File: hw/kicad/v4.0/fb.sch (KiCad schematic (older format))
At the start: 48 parts, among them J1 RJ45_LED, U15 SN65176B, U16 SN65176B, U19 SN65176B, U7 LM358

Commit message: Changed 120uf 1808 to 1210 100uF
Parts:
- C116, C117, C118, C12, C125, C37, C71, C73, C76: LCSC C14663 -> C14663
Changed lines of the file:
@@
 F 9 "" H 0   0   50  0001 C CNN "Description"
 F 10 "" H 0   0   50  0001 C CNN "Manufacturer"
-F 11 " C14663" H 9200 1250 50  0001 C CNN "LCSC"
+F 11 "C14663" H 9200 1250 50  0001 C CNN "LCSC"
 	1    9200 1250
 	1    0    0    -1
@@
 F 9 "" H 0   0   50  0001 C CNN "Description"
 F 10 "" H 0   0   50  0001 C CNN "Manufacturer"
-F 11 " C14663" H 9200 2650 50  0001 C CNN "LCSC"
+F 11 "C14663" H 9200 2650 50  0001 C CNN "LCSC"
 	1    9200 2650
 	1    0    0    -1
@@
 F 9 "" H 0   0   50  0001 C CNN "Description"
 F 10 "" H 0   0   50  0001 C CNN "Manufacturer"
-F 11 " C14663" H 9200 4050 50  0001 C CNN "LCSC"
+F 11 "C14663" H 9200 4050 50  0001 C CNN "LCSC"
 	1    9200 4050
 	1    0    0    -1
@@
 F 9 "" H 0   0   50  0001 C CNN "Description"
 F 10 "" H 0   0   50  0001 C CNN "Manufacturer"
-F 11 " C14663" H 2700 6800 50  0001 C CNN "LCSC"
+F 11 "C14663" H 2700 6800 50  0001 C CNN "LCSC"
 	1    2700 6800
 	1    0    0    -1
@@
 F 9 "" H 0   0   50  0001 C CNN "Description"
 F 10 "" H 0   0   50  0001 C CNN "Manufacturer"
-F 11 " C14663" H 3100 5750 50  0001 C CNN "LCSC"
+F 11 "C14663" H 3100 5750 50  0001 C CNN "LCSC"
 	1    3100 5750
 	-1   0    0    1
@@
 F 9 "" H 0   0   50  0001 C CNN "Description"
 F 10 "" H 0   0   50  0001 C CNN "Manufacturer"
-F 11 " C14663" H 1700 5500 50  0001 C CNN "LCSC"
+F 11 "C14663" H 1700 5500 50  0001 C CNN "LCSC"
 	1    1700 5500
 	-1   0    0    1
@@
 F 9 "" H 0   0   50  0001 C CNN "Description"
 F 10 "" H 0   0   50  0001 C CNN "Manufacturer"
-F 11 " C14663" H 10700 1050 50  0001 C CNN "LCSC"
+F 11 "C14663" H 10700 1050 50  0001 C CNN "LCSC"
 	1    10700 1050
 	1    0    0    1
@@
 F 9 "" H 0   0   50  0001 C CNN "Description"
 F 10 "" H 0   0   50  0001 C CNN "Manufacturer"
-F 11 " C14663" H 2500 3900 50  0001 C CNN "LCSC"
+F 11 "C14663" H 2500 3900 50  0001 C CNN "LCSC"
 	1    2500 3900
 	1    0    0    -1
@@
 F 9 "" H 0   0   50  0001 C CNN "Description"
 F 10 "" H 0   0   50  0001 C CNN "Manufacturer"
-F 11 " C14663" H 2450 4750 50  0001 C CNN "LCSC"
+F 11 "C14663" H 2450 4750 50  0001 C CNN "LCSC"
 	1    2450 4750
 	1    0    0    -1

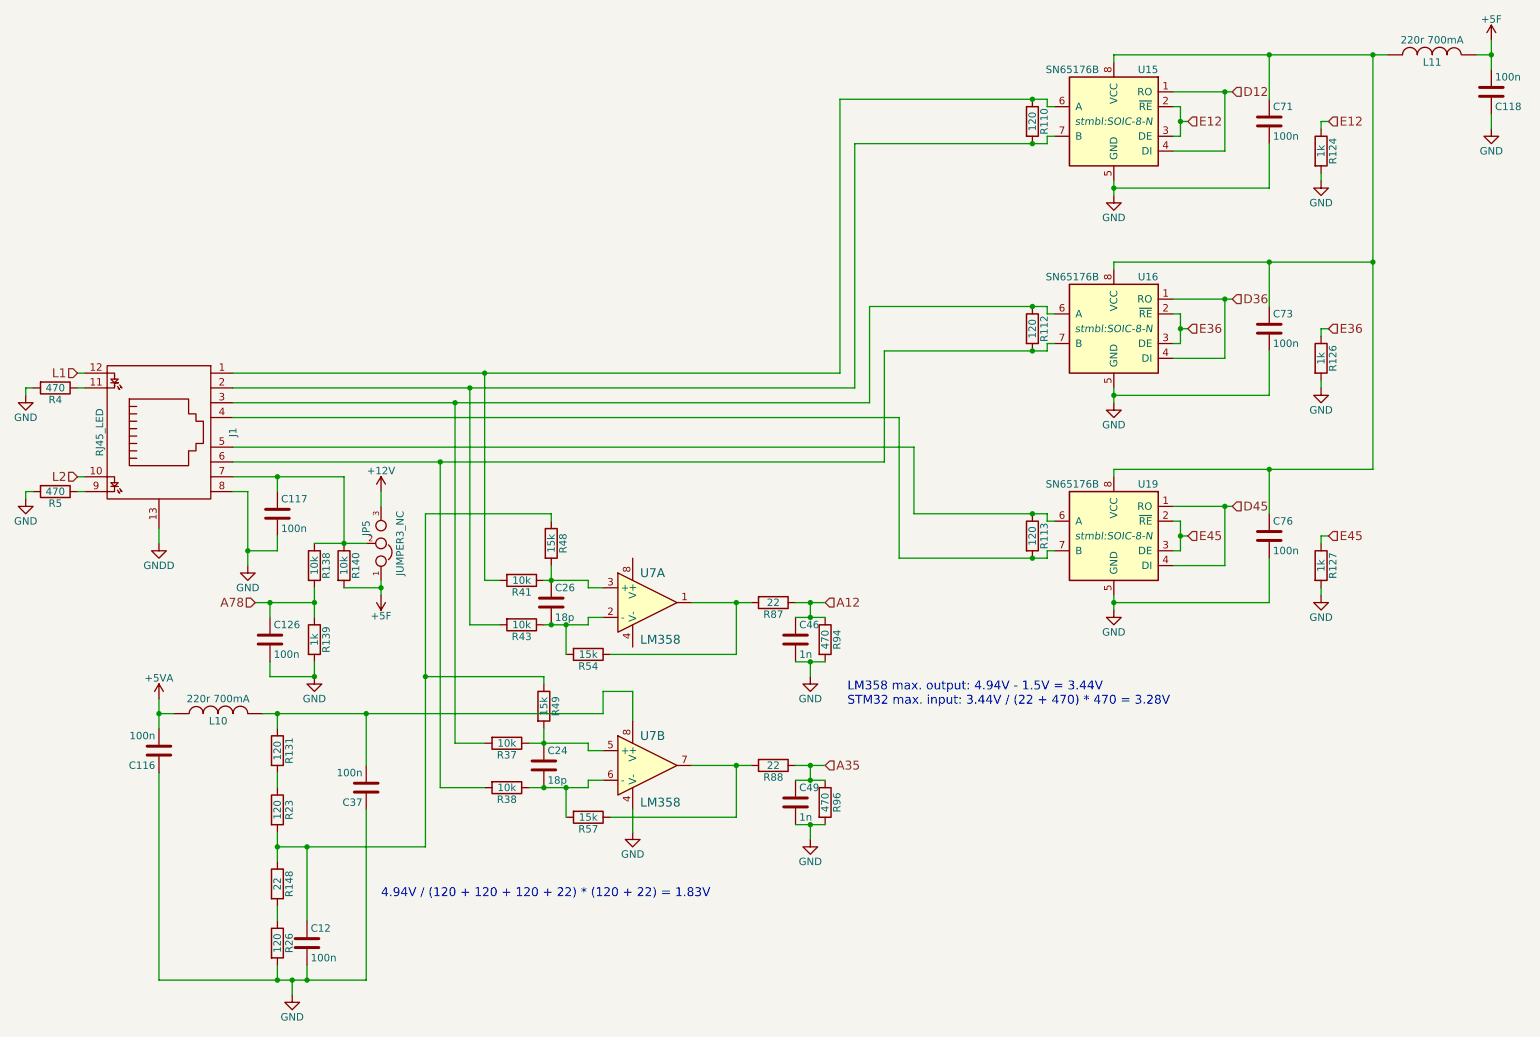
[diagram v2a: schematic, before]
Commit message: Switch some 2.2uf 0603 to 1uf bypass to get 50V version on jlcpcb
Change 2.2uf 0603 to 0805 on iram to get 50V version on jlcpcb
other cleanup
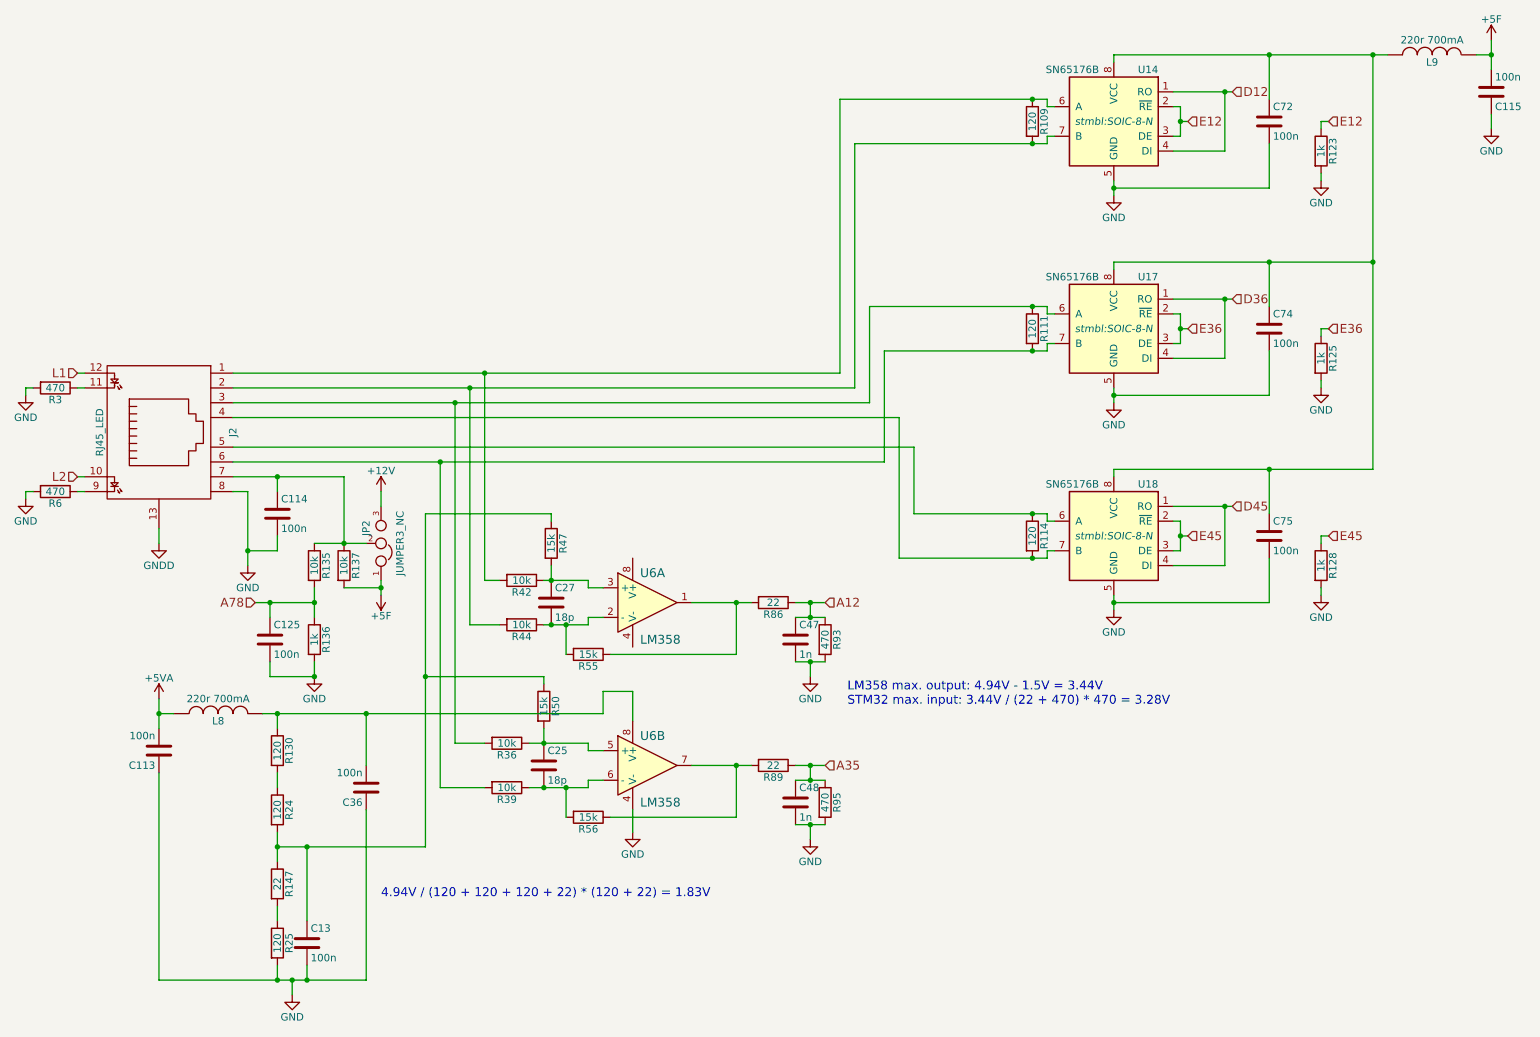
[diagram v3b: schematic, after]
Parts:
- C116, C117, C118, C12, C125, C37, C71, C73, C76: Manufacturer (none) -> YAGEO; Manufacturer No (none) -> CC0603KRX7R9BB104
- C24, C26: Manufacturer (none) -> Samsung Electro-Mechanics; Manufacturer No (none) -> CL10C180JB8NNNC
- C46, C49: Manufacturer (none) -> Samsung Electro-Mechanics; Manufacturer No (none) -> CL10B102KB8NNNC
- J1: LCSC C138392 -> (none)
